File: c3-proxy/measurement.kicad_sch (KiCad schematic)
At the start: 24 parts, among them Q4 DMP2035UQ-7, U1 MCP2221AxST, U5 TS5A21366, U6 MAX892LEUA+T, U7 MIC23050-SYML, U8 LTC4412xS6

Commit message: style and logic fixes
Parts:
- added C8, C9: 1uF, oresat-passives:0603-A, symbol Device:C_Small
- added D4: GREEN, oresat-passives:0603-A, symbol Device:LED
- added R7: 10k, oresat-passives:0603-A, symbol Device:R_Small_US
- added TP24, TP25, TP26, TP27: Test-Point, oresat-misc:TestPoint-0.75mm-th, symbol oresat_stuff:Test-Point-0.75mm-th
- R13, R14: value 1k -> 10k
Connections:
- net 3.3V: now also C8.1, D4.2 (A), TP26.1, TP27.1
- net GND: now also C8.2, C9.2, R7.2
- net OPD_PWR: now also TP25.1
- net at Q4.1 (D), U5.3 (IN2), U5.7 (IN1)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: now also C9.1
- net at U6.6 (~{FAULT}): now also TP24.1
- new net: D4.1 (K), R7.1
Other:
- moved on the sheet: C3, C4, C5, L1, Q4, R12, TP22, TP23, U7, U8

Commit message: final layout and schematic touch ups
killed buzzer
deleted old folder
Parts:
- C1, C3, C4, C6: DIST (none) -> DigiKey; DPN (none) -> 490-GRT188C71C475KE13DCT-ND; MFR (none) -> Murata Electronics; MPN (none) -> GRT188C71C475KE13D
- C5: value 470uF -> 470pF; DIST (none) -> DigiKey; DPN (none) -> 399-6894-1-ND; MFR (none) -> KEMET; MPN (none) -> C0603C471K5RACAUTO
- C8, C9: DIST (none) -> DigiKey; DPN (none) -> 490-GRT188R71E105KE13DCT-ND; MFR (none) -> Murata Electronics; MPN (none) -> GRT188R71E105KE13D
- D1, D4: DIST (none) -> DigiKey; DPN (none) -> 732-4971-1-ND; MFR (none) -> Wurth; MPN (none) -> 150060GS75000
- D2: DIST (none) -> DigiKey; DPN (none) -> 732-150060AS75000CT-ND; MFR (none) -> Wurth; MPN (none) -> 150060AS75000
- D3: value GRN -> GREEN; DIST (none) -> DigiKey; DPN (none) -> 732-4971-1-ND; MFR (none) -> Wurth; MPN (none) -> 150060GS75000
- L1: DIST (none) -> DigiKey; DPN (none) -> 445-8657-2-ND; MFR (none) -> TDK; MPN (none) -> MLZ2012M1R0HT000
- Q4: DIST (none) -> DigiKey; DPN (none) -> 31-DMP2035UQ-7CT-ND; MFR (none) -> Diodes Incorporated; MPN (none) -> DMP2035UQ-7
- R10, R9: DIST (none) -> DigiKey; DPN (none) -> RMCF0603FT4K70CT-ND; MFR (none) -> Stackpole Electronics; MPN (none) -> RMCF0603FT4K70
- R12, R13, R14, R5, R7: DIST (none) -> DigiKey; DPN (none) -> RMCF0603FT10K0CT-ND; MFR (none) -> Stackpole Electronics; MPN (none) -> RMCF0603FT10K0
- R4: DIST (none) -> DigiKey; DPN (none) -> RMCF0603FT23K7CT-ND; MFR (none) -> Stackpole; MPN (none) -> RMCF0603FT23K7
- U1: DIST (none) -> DigiKey; DPN (none) -> MCP2221AT-I/STTR-ND; MFR (none) -> Microchip Technology; MPN (none) -> MCP2221AT-I/ST
- U5: DIST (none) -> DigiKey; DPN (none) -> 296-24304-1-ND; MFR (none) -> Texas Instruments; MPN (none) -> TS5A21366DCUR
- U6: DIST (none) -> DigiKey; DPN (none) -> MAX892LEUA+-ND; MFR (none) -> Analog Devices; MPN (none) -> MAX892LEUA+T
- U7: DIST (none) -> DigiKey; DPN (none) -> 576-3351-2-ND; MFR (none) -> Microchip Technology; MPN (none) -> MIC23050-SYML-TR
- U8: DIST (none) -> DigiKey; DPN (none) -> LTC4412ES6#WTRMPBF; MFR (none) -> Analog Devices; MPN (none) -> LTC4412ES6#PBF
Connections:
- net 3.3V: now also U1.4 (~{RST})
- no-connect marks 1 -> 0
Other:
- note added: "reversed PMOS for ideal diode"

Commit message: Fix library paths and start fixing ERCs
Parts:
- TP22, TP23, TP24, TP25, TP26, TP27: symbol oresat_stuff:Test-Point-0.75mm-th -> oresat-misc:Test-Point-0.75mm-th
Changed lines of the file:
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@@
 	)
 	(symbol
-		(lib_id "oresat_stuff:Test-Point-0.75mm-th")
+		(lib_id "oresat-misc:Test-Point-0.75mm-th")
 		(at 170.18 74.93 0)
 		(unit 1)
@@
 	)
 	(symbol
-		(lib_id "oresat_stuff:Test-Point-0.75mm-th")
+		(lib_id "oresat-misc:Test-Point-0.75mm-th")
 		(at 288.29 95.25 0)
 		(unit 1)
@@
 	)
 	(symbol
-		(lib_id "oresat_stuff:Test-Point-0.75mm-th")
+		(lib_id "oresat-misc:Test-Point-0.75mm-th")
 		(at 156.21 74.93 0)
 		(unit 1)
@@
 	)
 	(symbol
-		(lib_id "oresat_stuff:VBUS")
+		(lib_id "power:VBUS")
 		(at 156.21 146.05 0)
 		(mirror y)
@@
 	)
 	(symbol
-		(lib_id "oresat_stuff:VBUS")
+		(lib_id "power:VBUS")
 		(at 257.81 129.54 0)
 		(unit 1)
@@
 	)
 	(symbol
-		(lib_id "oresat_stuff:Test-Point-0.75mm-th")
+		(lib_id "oresat-misc:Test-Point-0.75mm-th")
 		(at 199.39 87.63 0)
 		(unit 1)
@@
 	)
 	(symbol
-		(lib_id "oresat_stuff:VBUS")
+		(lib_id "power:VBUS")
 		(at 217.17 128.27 0)
 		(unit 1)
@@
 	)
 	(symbol
-		(lib_id "oresat_stuff:Test-Point-0.75mm-th")
+		(lib_id "oresat-misc:Test-Point-0.75mm-th")
 		(at 260.35 95.25 0)
 		(unit 1)
@@
 	)
 	(symbol
-		(lib_id "oresat_stuff:VBUS")
+		(lib_id "power:VBUS")
 		(at 109.22 71.12 0)
 		(unit 1)
@@
 	)
 	(symbol
-		(lib_id "oresat_stuff:Test-Point-0.75mm-th")
+		(lib_id "oresat-misc:Test-Point-0.75mm-th")
 		(at 306.07 74.93 0)
 		(unit 1)

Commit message: did like... everything...
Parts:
- removed TP22, TP23: Test-Point, oresat-misc:TestPoint-0.75mm-th, symbol oresat-misc:Test-Point-0.75mm-th
- added SW2: SW_DP3T, oresat-misc:CL-SB-23B-XX, symbol Switch:SW_DP3T
- C1: value 4.7uF -> 1uF
- C3, C4: footprint oresat-passives:0603-A -> oresat-passives:0805-A
- C6: value 4.7uF -> 100n
- D3: value GREEN -> AMB; DPN 732-4971-1-ND -> 732-150060AS75000CT-ND; MPN 150060GS75000 -> 150060AS75000
- U5: symbol oresat_stuff:TS5A21366 -> oresat-ics:TS5A21366; DIS (none) -> DigiKey
- U6: symbol oresat_stuff:MAX892LEUA+T -> oresat-ics:MAX892LEUA+T
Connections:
- net 3.3V: now also R13.2, R14.2
- net C3-UART-RX: now also SW2.1, SW2.8; no longer U1.5 (URx)
- net C3-UART-TX: now also SW2.4, SW2.5; no longer U1.6 (UTx)
- net GND: no longer R13.2, R14.2
- net at R14.1: now also D3.2 (A); no longer D3.1 (K)
- net at U1.2 (GP0): now also D3.1 (K); no longer D3.2 (A)
- net at U1.3 (GP1): now also D2.1 (K); no longer D2.2 (A)
- net at R13.1: now also D2.2 (A); no longer D2.1 (K)
- new net MCP_URx: SW2.3, U1.5 (URx)
- new net MCP_UTx: SW2.7, U1.6 (UTx)
- no-connect marks 0 -> 4
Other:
- note added: "0) act like a c3 (rx->rx, tx->tx) 1) disconnect uarts 2) act like a card (rx->tx, tx->rx)"
- note added: "GP0/1 are set to active low UART indicators in flash"
- note removed: "GP0/1 default to being UART indicators, can be changed in flash"
- note removed: "I can't find if these pins are active high or active low when in UART LED mode"
- note removed: "mux to swap the UART linesto listen to other C3?"
- moved on the sheet: C1, C6, D2, D3, R13, R14, U1

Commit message: v1.0 of the C3 Proxy sent off to fabrication.
Added makefile and README. Fixed a bunch of BOM issues, mostly just EOL and out of stock components. Fixed wrong footprints in the BOM, and switched diode from TH to SMT. Cleaned up some traces for funsies,
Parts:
- C1: value 1uF -> 1u; DPN 490-GRT188C71C475KE13DCT-ND -> 490-GRT188R71E105KE13DCT-ND; MPN GRT188C71C475KE13D -> GRT188R71E105KE13D
- C3, C4: value 4.7uF -> 4.7u; DPN 490-GRT188C71C475KE13DCT-ND -> 490-GRT21BC71E475KE13LCT-ND; MPN GRT188C71C475KE13D -> GRT21BC71E475KE13L
- C5: value 470pF -> 470p
- C6: DPN 490-GRT188C71C475KE13DCT-ND -> 399-6856-1-ND; MFR Murata Electronics -> KEMET; MPN GRT188C71C475KE13D -> C0603C104K5RACAUTO
- C8, C9: value 1uF -> 1u
- D1, D4: value GREEN -> GRN
- L1: DPN 445-8657-2-ND -> 445-8657-1-ND
- SW2: DIS (none) -> DigiKey; DIST (none) -> DigiKey; DPN (none) -> 563-1355-1-ND; MFR (none) -> Nidec Components; MPN (none) -> CL-SB-23B-02T
- SW2: footprint (none) -> oresat-misc:CL-SB-23B-XX; DIS (none) -> DigiKey; DIST (none) -> DigiKey; DPN (none) -> 563-1355-1-ND; MFR (none) -> Nidec Components; MPN (none) -> CL-SB-23B-02T
- U1: DPN MCP2221AT-I/STTR-ND -> MCP2221AT-I/STCT-ND
- U7: DPN 576-3351-2-ND -> 576-3351-1-ND
- U8: DPN LTC4412ES6#WTRMPBF -> 505-LTC4412ES6#WTRMPBFCT-ND; MPN LTC4412ES6#PBF -> LTC4412ES6#WTRMPBF
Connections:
- net 3.3V: now also R13.1, R14.1; no longer R13.2, R14.2
- net at D3.2 (A): now also R14.2; no longer R14.1
- net at D2.2 (A): now also R13.2; no longer R13.1
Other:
- note added: "1) act like a c3 (rx->rx, tx->tx) 2) disconnect uarts 3) act like a card (rx->tx, tx->rx)"
- note added: "3.3V"
- note added: "Ideal diode for OPD_PWR"
- note added: "OPD"
- note added: "RX"
- note added: "TX"
- note removed: "0) act like a c3 (rx->rx, tx->tx) 1) disconnect uarts 2) act like a card (rx->tx, tx->rx)"
- note removed: "reversed PMOS for ideal diode"
- moved on the sheet: C5, R13, R14

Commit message: decreased size to fit in EU, transistor orientation
changed DC jack to be edge connected.
adjusted layout in top-right corner to still fit mounting hole.
fixed transistor orientation by switching to GSD symbols
moved SW2 and clarified silkscreen with boxes
changed via sizes to be standardized
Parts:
- removed Q4: DMP2035UQ-7, Package_TO_SOT_SMD:SOT-23-3, symbol Simulation_SPICE:PMOS
- added Q8: DMP2035UQ-7, Package_TO_SOT_SMD:SOT-23-3, symbol Transistor_FET:Q_PMOS_GSD
- R13, R14: value 10k -> 4.7k
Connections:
- net OPD_PWR: now also Q8.2 (S)
- net at C9.1, U5.3 (IN2), U5.7 (IN1)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: now also Q8.3 (D)
- net at U8.5 (GATE): now also Q8.1 (G)
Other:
- title: Flatsat Interface Card -> c3-Proxy card
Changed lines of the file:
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@@
 	(paper "B")
 	(title_block
-		(title "Flatsat Interface Card")
-		(date "2026-06-29")
+		(title "c3-Proxy card")
+		(date "2026-09-07")
 		(rev "${REVISION}")
 		(company "Portland State Aerospace Society")
@@
 	)
 	(symbol
-		(lib_id "Simulation_SPICE:PMOS")
+		(lib_id "Transistor_FET:Q_PMOS_GSD")
 		(at 274.32 77.47 90)
 		(unit 1)
@@
 		(in_pos_files yes)
 		(dnp no)
-		(property "Reference" "Q4"
+		(fields_autoplaced yes)
+		(property "Reference" "Q8"
 			(at 274.32 68.58 90)
 			(show_name no)
@@
 		)
 		(property "Datasheet" "https://www.diodes.com/assets/Datasheets/DMP2035U.pdf"
-			(at 287.02 77.47 0)
+			(at 274.32 77.47 0)
 			(hide yes)
 			(show_name no)
@@
 		)
 		(property "Sim.Device" "PMOS"
-			(at 291.465 77.47 0)
+			(at 274.32 77.47 90)
 			(hide yes)
 			(show_name no)
@@
 		)
 		(property "Sim.Type" "VDMOS"
-			(at 293.37 77.47 0)
+			(at 274.32 77.47 90)
 			(hide yes)
 			(show_name no)
@@
 			)
 		)
-		(property "Sim.Pins" "1=D 2=G 3=S"
-			(at 289.56 77.47 0)
+		(property "Sim.Pins" ""
+			(at 274.32 77.47 90)
 			(hide yes)
 			(show_name no)
@@
 		(pin "3"
 		)
-		(pin "1"
-		)
 		(pin "2"
 		)
+		(pin "1"
+		)
 		(instances
 			(project "c3-proxy"
 				(path "/1a9202c4-e698-4c93-952c-ee3e64e9e49c/ad201ad7-0b68-497a-9bd5-92d5158f3b08"
-					(reference "Q4")
+					(reference "Q8")
 					(unit 1)
 				)
@@
 			)
 		)
-		(property "Value" "10k"
+		(property "Value" "4.7k"
 			(at 176.53 141.732 0)
 			(show_name no)
@@
 			)
 		)
-		(property "Value" "10k"
+		(property "Value" "4.7k"
 			(at 188.214 141.732 0)
 			(show_name no)

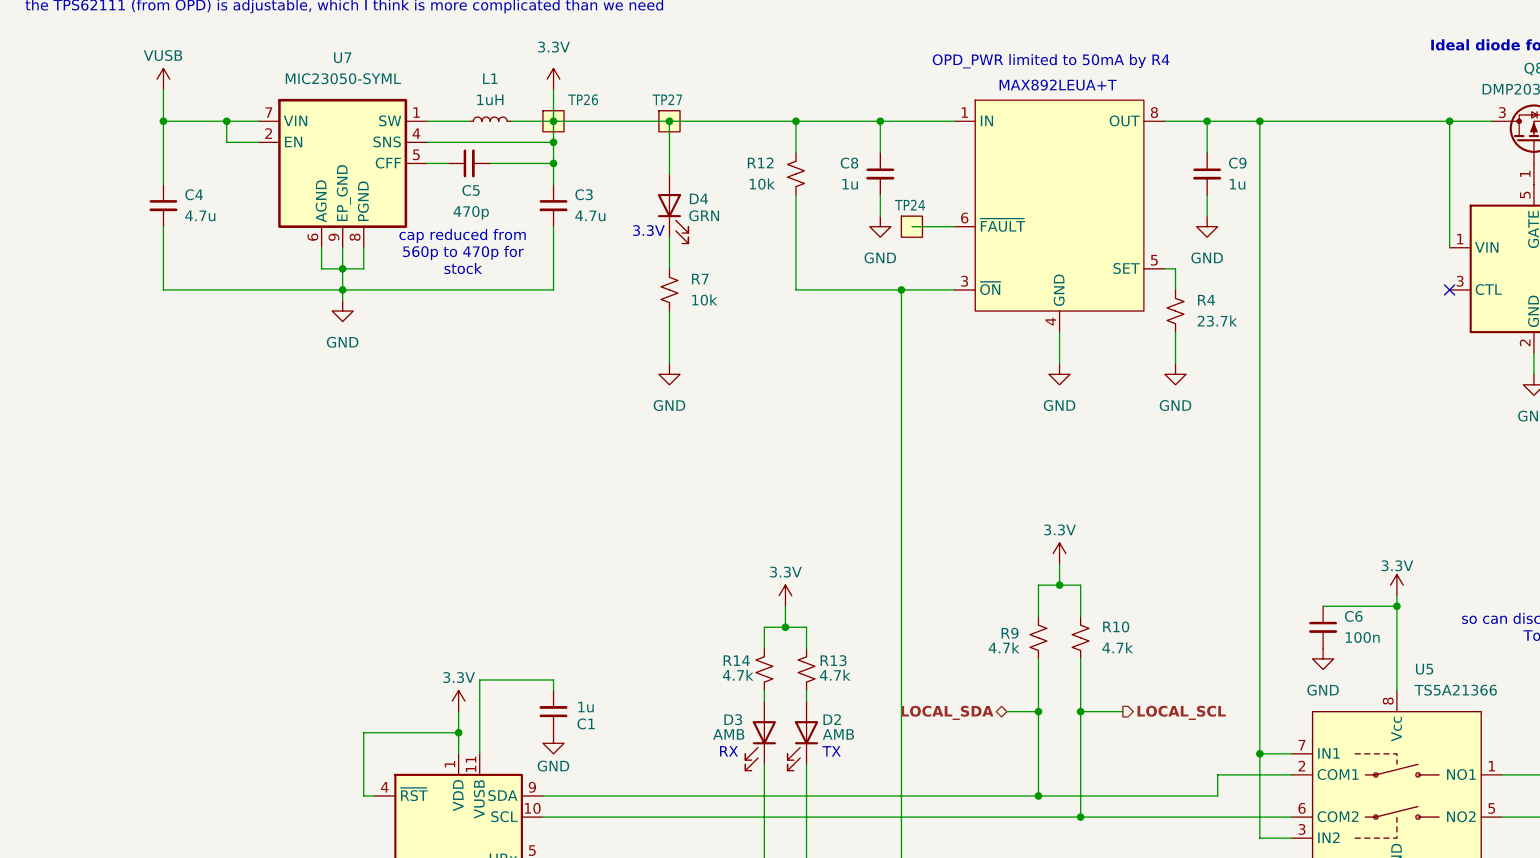
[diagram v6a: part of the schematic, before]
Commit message: changed footprints in schematic
so that "update from schematic" doesn't kill my baby resistors
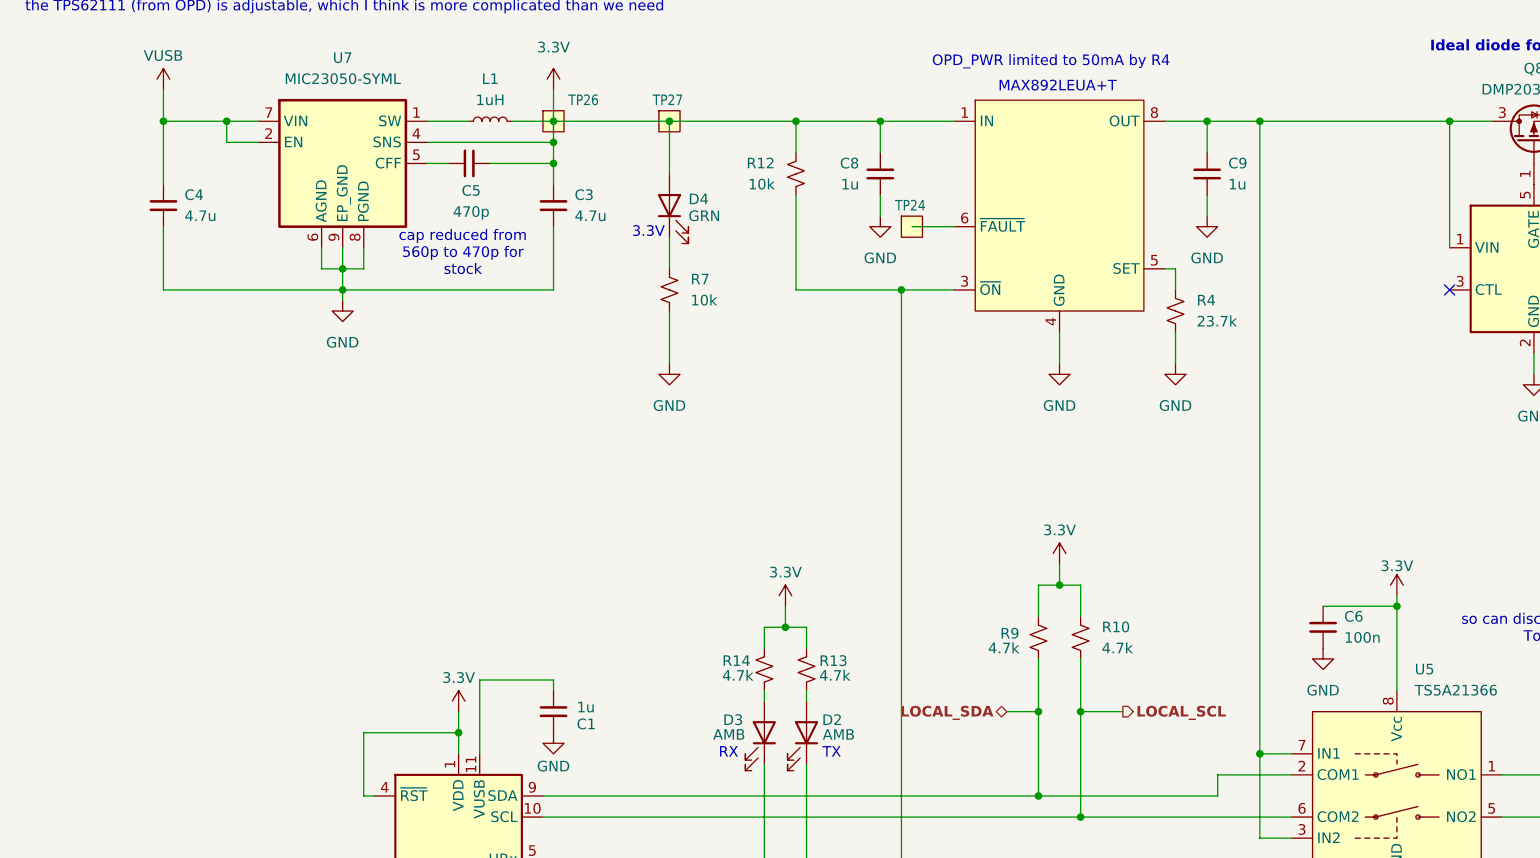
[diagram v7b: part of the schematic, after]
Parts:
- C1, C8, C9: footprint oresat-passives:0603-A -> oresat-passives:0603-C-NOSILK; DIST DigiKey -> (none); DPN 490-GRT188R71E105KE13DCT-ND -> (none); MFR Murata Electronics -> (none); MPN GRT188R71E105KE13D -> (none)
- C3, C4: footprint oresat-passives:0805-A -> oresat-passives:0805-C-NOSILK; DIST DigiKey -> (none); DPN 490-GRT21BC71E475KE13LCT-ND -> (none); MFR Murata Electronics -> (none); MPN GRT21BC71E475KE13L -> (none)
- C5: footprint oresat-passives:0603-A -> oresat-passives:0603-C-NOSILK; DIST DigiKey -> (none); DPN 399-6894-1-ND -> (none); MFR KEMET -> (none); MPN C0603C471K5RACAUTO -> (none)
- C6: footprint oresat-passives:0603-A -> oresat-passives:0603-C-NOSILK; DIST DigiKey -> (none); DPN 399-6856-1-ND -> (none); MFR KEMET -> (none); MPN C0603C104K5RACAUTO -> (none)
- D1, D2, D3, D4, R10, R12, R13, R14, R4, R5, R7, R9: footprint oresat-passives:0603-A -> oresat-passives:0603-C-NOSILK
- L1: footprint oresat-passives:0805-A -> oresat-passives:0805-C-NOSILK

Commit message: fixed BOM, silk art scale
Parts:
- C1, C8, C9: DIST (none) -> DigiKey; DPN (none) -> 490-GRT188R71E105KE13DCT-ND; MFR (none) -> Murata Electronics; MPN (none) -> GRT188R71E105KE13D
- C3, C4: DIST (none) -> DigiKey; DPN (none) -> 490-GRT21BC71E475KE13LCT-ND; MFR (none) -> Murata Electronics; MPN (none) -> GRT21BC71E475KE13L
- C5: DIST (none) -> DigiKey; DPN (none) -> 399-6894-1-ND; MFR (none) -> KEMET; MPN (none) -> C0603C471K5RACAUTO
- C6: DIST (none) -> DigiKey; DPN (none) -> 399-6856-1-ND; MFR (none) -> KEMET; MPN (none) -> C0603C104K5RACAUTO
